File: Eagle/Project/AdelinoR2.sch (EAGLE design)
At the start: 70 parts, among them J1 DC-044-A, J2 YELLOW-8P-2.54, J3 YELLOW-6P-2.54, J4 YELLOW-8P-2.54, J5 YELLOW-8P-2.54, J6 4P-2.0, J7 YELLOW-2X3P-2.54, J8 4P-2.0, Q1 NCE3407A, Q2 CJ2305, SW1 TS-1101F, U1 MP1496DJ-SOT23-8, U2 CJT1117-3.3-SOT223, U3 ESP-12F / OPL: 317060163 / SM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, U4 ATMEGA32U4-MUR-QFN44, U5 74VHC125MTCX-TSSOP14, U6 ATMEGA32U4-TQFP44, X1 306010049_XTAL_16MHZ-3225_4P

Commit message: Power supply routing wip.
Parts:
- removed L3: 303010525_22UH_7.1X6.6MM, Seeed-OPL-2017-01-Inductor-Akita:303010525_22UH_7.1X6.6MM
- removed R14: 10K / 1%, Seeed-Resistor:SMD-RES-10K-1%-1/10W(0603)
- removed R16: 30K / 1%, Seeed-Resistor:SMD-RES-30K-1%-1/10W(0603)
- L2: device Seeed-Inductor:SMD-INDUCTOR-10UH-225MA-10%(0806) -> Seeed-Inductor:SMD-INDUCTOR-10UH-20%-2.35A(2P-5X5X4MM)
- R13: value 68K / 1% -> 2K7 / 1%; device Seeed-Resistor:SMD-RES-68K-1%-1/10W(0603) -> Seeed-Resistor:SMD-RES-2.7K-1%-1/10W(0603); R (none) -> 2K7 / 1%
- R15: device Seeed-Resistor:SMD-RES-3K-1%-1/10W(0603) -> Seeed-Resistor:SMD-RES-510R-1%-1/10W(0603); R (none) -> 510R / 1%
- R18: value 3K / 1% -> 3.3K; device Seeed-Resistor:SMD-RES-3K-1%-1/10W(0603) -> Seeed-Resistor:SMD-RES-3.3K-5%-1/16W(0402)
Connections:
- net N$10 renamed SW_VCC_IN
- net N$12 renamed SW_VCAP
- net N$14 renamed SW_BS
- net N$19 renamed SW_VCC_OUT
- net N$20 renamed SW_EN
- net N$24 renamed SW_FB
- net N$4 renamed SW_SS
- removed net N$21: R16.1, R18.2
- removed net N$22: R14.1, R15.2
- net N$23: now also R15.2, R18.2; no longer R14.2, R16.2
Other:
- moved on the sheet: R15
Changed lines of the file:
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@@
 <setting verticaltext="up"/>
 </settings>
-<grid distance="0.05" unitdist="inch" unit="inch" style="lines" multiple="1" display="no" altdistance="0.01" altunitdist="inch" altunit="inch"/>
+<grid distance="0.1" unitdist="inch" unit="inch" style="lines" multiple="1" display="no" altdistance="0.01" altunitdist="inch" altunit="inch"/>
 <layers>
 <layer number="1" name="Top" color="4" fill="1" visible="no" active="no"/>
@@
 <classes>
 <class number="0" name="default" width="0.254" drill="0.6096">
-<clearance class="0" value="0.254"/>
+<clearance class="0" value="0.2032"/>
 </class>
 </classes>
@@
 <part name="R6" library="Seeed-Resistor" deviceset="SMD-RES-10R-1%-1/16W(0402)" device="" value="10R 1/16W"/>
 <part name="C5" library="Seeed-Capacitor" deviceset="CERAMIC-100NF-25V-10%-X7R(0402)" device="" value="100nf"/>
-<part name="L2" library="Seeed-Inductor" deviceset="SMD-INDUCTOR-10UH-225MA-10%(0806)" device="" value="10UH-225MA"/>
+<part name="L2" library="Seeed-Inductor" deviceset="SMD-INDUCTOR-10UH-20%-2.35A(2P-5X5X4MM)" device="" value="10UH-225MA"/>
 <part name="R7" library="Seeed-Resistor" deviceset="SMD-RES-100K-1%-1/16W(0402)" device="" value="100K"/>
-<part name="R13" library="Seeed-Resistor" deviceset="SMD-RES-68K-1%-1/10W(0603)" device="" value="68K / 1%"/>
-<part name="R14" library="Seeed-Resistor" deviceset="SMD-RES-10K-1%-1/10W(0603)" device="" value="10K / 1%"/>
+<part name="R13" library="Seeed-Resistor" deviceset="SMD-RES-2.7K-1%-1/10W(0603)" device="" value="2K7 / 1%">
+<attribute name="R" value="2K7 / 1%"/>
+</part>
 <part name="GND15" library="supply1" library_urn="urn:adsk.eagle:library:371" deviceset="GND" device=""/>
-<part name="R16" library="Seeed-Resistor" deviceset="SMD-RES-30K-1%-1/10W(0603)" device="" value="30K / 1%"/>
 <part name="C19" library="Seeed-Capacitor" deviceset="CERAMIC-10UF-25V-10%-X5R(0805)" device="" value="10uf"/>
 <part name="C20" library="Seeed-Capacitor" deviceset="CERAMIC-10UF-25V-10%-X5R(0805)" device="" value="10uf"/>
-<part name="R15" library="Seeed-Resistor" deviceset="SMD-RES-3K-1%-1/10W(0603)" device="" value="3K / 1%"/>
-<part name="R18" library="Seeed-Resistor" deviceset="SMD-RES-3K-1%-1/10W(0603)" device="" value="3K / 1%"/>
+<part name="R15" library="Seeed-Resistor" deviceset="SMD-RES-510R-1%-1/10W(0603)" device="" value="3K / 1%">
+<attribute name="R" value="510R / 1%"/>
+</part>
+<part name="R18" library="Seeed-Resistor" deviceset="SMD-RES-3.3K-5%-1/16W(0402)" device="" value="3.3K"/>
 <part name="U6" library="Seeed-IC" deviceset="MCU-ATMEGA32U4-AU(TQFP44)" device="" value="ATMEGA32U4-TQFP44">
 <attribute name="DESC" value="SOCKET B - TQFP44"/>
 </part>
-<part name="L3" library="Seeed-OPL-2017-01-Inductor-Akita" deviceset="303010525_22UH_7.1X6.6MM" device=""/>
 <part name="GND2" library="supply1" library_urn="urn:adsk.eagle:library:371" deviceset="GND" device=""/>
 <part name="P+8" library="supply1" library_urn="urn:adsk.eagle:library:371" deviceset="+5V" device=""/>
@@
 <attribute name="VALUE" x="-123.19" y="148.59" size="1.27" layer="96" ratio="10" rot="R90"/>
 </instance>
-<instance part="L2" gate="L" x="-113.03" y="143.51" smashed="yes">
+<instance part="L2" gate="G$1" x="-113.03" y="143.51" smashed="yes">
 <attribute name="NAME" x="-116.84" y="144.78" size="1.27" layer="95" ratio="10"/>
-<attribute name="VALUE" x="-116.84" y="140.97" size="1.27" layer="96" ratio="10"/>
 </instance>
 <instance part="R7" gate="G$1" x="-170.18" y="143.51" smashed="yes" rot="R180">
@@
 <instance part="R13" gate="G$1" x="-113.03" y="137.16" smashed="yes">
 <attribute name="NAME" x="-116.84" y="138.43" size="1.27" layer="95" ratio="10"/>
-<attribute name="VALUE" x="-116.84" y="134.62" size="1.27" layer="96" ratio="10"/>
-</instance>
-<instance part="R14" gate="G$1" x="-134.62" y="128.27" smashed="yes">
-<attribute name="NAME" x="-138.43" y="129.54" size="1.27" layer="95" ratio="10"/>
-<attribute name="VALUE" x="-138.43" y="125.73" size="1.27" layer="96" ratio="10"/>
+<attribute name="R" x="-116.84" y="134.62" size="1.27" layer="96"/>
 </instance>
 <instance part="GND15" gate="1" x="-152.4" y="115.57" smashed="yes">
 <attribute name="VALUE" x="-154.94" y="113.03" size="1.778" layer="96"/>
-</instance>
-<instance part="R16" gate="G$1" x="-125.73" y="137.16" smashed="yes">
-<attribute name="NAME" x="-129.54" y="138.43" size="1.27" layer="95" ratio="10"/>
-<attribute name="VALUE" x="-129.54" y="134.62" size="1.27" layer="96" ratio="10"/>
 </instance>
 <instance part="C19" gate="G$1" x="-99.06" y="137.16" smashed="yes" rot="R90">
@@
 <attribute name="VALUE" x="-91.44" y="134.62" size="1.27" layer="96" ratio="10"/>
 </instance>
-<instance part="R15" gate="G$1" x="-144.78" y="128.27" smashed="yes">
-<attribute name="NAME" x="-148.59" y="129.54" size="1.27" layer="95" ratio="10"/>
-<attribute name="VALUE" x="-148.59" y="125.73" size="1.27" layer="96" ratio="10"/>
+<instance part="R15" gate="G$1" x="-134.62" y="128.27" smashed="yes">
+<attribute name="NAME" x="-138.43" y="129.54" size="1.27" layer="95" ratio="10"/>
+<attribute name="R" x="-138.43" y="125.73" size="1.27" layer="96"/>
 </instance>
 <instance part="R18" gate="G$1" x="-134.62" y="137.16" smashed="yes">
@@
 <attribute name="VALUE" x="201.93" y="135.89" size="1.778" layer="96"/>
 <attribute name="DESC" x="201.93" y="133.35" size="1.778" layer="96"/>
-</instance>
-<instance part="L3" gate="G$1" x="-137.16" y="165.1" smashed="yes">
-<attribute name="NAME" x="-142.24" y="167.64" size="1.778" layer="97"/>
-<attribute name="VALUE" x="-142.24" y="162.56" size="1.778" layer="96"/>
 </instance>
 <instance part="GND2" gate="1" x="163.83" y="50.8" smashed="yes">
@@
 <junction x="-99.06" y="121.92"/>
 <pinref part="R15" gate="G$1" pin="1"/>
-<wire x1="-148.59" y1="128.27" x2="-152.4" y2="128.27" width="0.1524" layer="91"/>
+<wire x1="-138.43" y1="128.27" x2="-152.4" y2="128.27" width="0.1524" layer="91"/>
 <junction x="-152.4" y="128.27"/>
 <pinref part="C3" gate="G$1" pin="1"/>
@@
 <wire x1="-92.71" y1="143.51" x2="-86.36" y2="143.51" width="0.1524" layer="91"/>
 <junction x="-86.36" y="143.51"/>
-<pinref part="L2" gate="L" pin="2"/>
+<pinref part="L2" gate="G$1" pin="2"/>
 <wire x1="-107.95" y1="143.51" x2="-105.41" y2="143.51" width="0.1524" layer="91"/>
 <wire x1="-105.41" y1="143.51" x2="-99.06" y2="143.51" width="0.1524" layer="91"/>
@@
 </segment>
 </net>
-<net name="N$10" class="0">
+<net name="SW_VCC_IN" class="0">
 <segment>
 <pinref part="Q1" gate="G$1" pin="S"/>
@@
 </segment>
 </net>
-<net name="N$12" class="0">
+<net name="SW_VCAP" class="0">
 <segment>
 <pinref part="U1" gate="G$1" pin="VCC"/>
@@
 </segment>
 </net>
-<net name="N$14" class="0">
+<net name="SW_BS" class="0">
 <segment>
 <pinref part="U1" gate="G$1" pin="BS"/>
@@
 </segment>
 </net>
-<net name="N$19" class="0">
+<net name="SW_VCC_OUT" class="0">
 <segment>
 <pinref part="U1" gate="G$1" pin="SW"/>
-<pinref part="L2" gate="L" pin="1"/>
+<pinref part="L2" gate="G$1" pin="1"/>
 <wire x1="-140.97" y1="143.51" x2="-119.38" y2="143.51" width="0.1524" layer="91"/>
 <pinref part="C5" gate="G$1" pin="1"/>
@@
 <wire x1="-119.38" y1="147.32" x2="-119.38" y2="143.51" width="0.1524" layer="91"/>
 <junction x="-119.38" y="143.51"/>
-</segment>
-</net>
-<net name="N$20" class="0">
+<label x="-128.27" y="143.51" size="0.8128" layer="95"/>
+</segment>
+</net>
+<net name="SW_EN" class="0">
 <segment>
 <pinref part="U1" gate="G$1" pin="EN/SYNC"/>
@@
 <net name="N$23" class="0">
 <segment>
-<pinref part="R16" gate="G$1" pin="2"/>
 <pinref part="R13" gate="G$1" pin="1"/>
-<wire x1="-116.84" y1="137.16" x2="-119.38" y2="137.16" width="0.1524" layer="91"/>
-<pinref part="R14" gate="G$1" pin="2"/>
-<wire x1="-119.38" y1="137.16" x2="-121.92" y2="137.16" width="0.1524" layer="91"/>
+<pinref part="R18" gate="G$1" pin="2"/>
+<wire x1="-130.81" y1="137.16" x2="-119.38" y2="137.16" width="0.1524" layer="91"/>
+<pinref part="R15" gate="G$1" pin="2"/>
+<wire x1="-119.38" y1="137.16" x2="-116.84" y2="137.16" width="0.1524" layer="91"/>
 <wire x1="-130.81" y1="128.27" x2="-119.38" y2="128.27" width="0.1524" layer="91"/>
 <wire x1="-119.38" y1="128.27" x2="-119.38" y2="137.16" width="0.1524" layer="91"/>
@@
 </segment>
 </net>
-<net name="N$22" class="0">
-<segment>
-<pinref part="R14" gate="G$1" pin="1"/>
-<pinref part="R15" gate="G$1" pin="2"/>
-<wire x1="-138.43" y1="128.27" x2="-140.97" y2="128.27" width="0.1524" layer="91"/>
-</segment>
-</net>
-<net name="N$4" class="0">
+<net name="SW_SS" class="0">
 <segment>
 <pinref part="C3" gate="G$1" pin="2"/>
@@
 </segment>
 </net>
-<net name="N$21" class="0">
-<segment>
-<pinref part="R16" gate="G$1" pin="1"/>
-<pinref part="R18" gate="G$1" pin="2"/>
-<wire x1="-129.54" y1="137.16" x2="-130.81" y2="137.16" width="0.1524" layer="91"/>
-</segment>
-</net>
-<net name="N$24" class="0">
+<net name="SW_FB" class="0">
 <segment>
 <pinref part="R18" gate="G$1" pin="1"/>

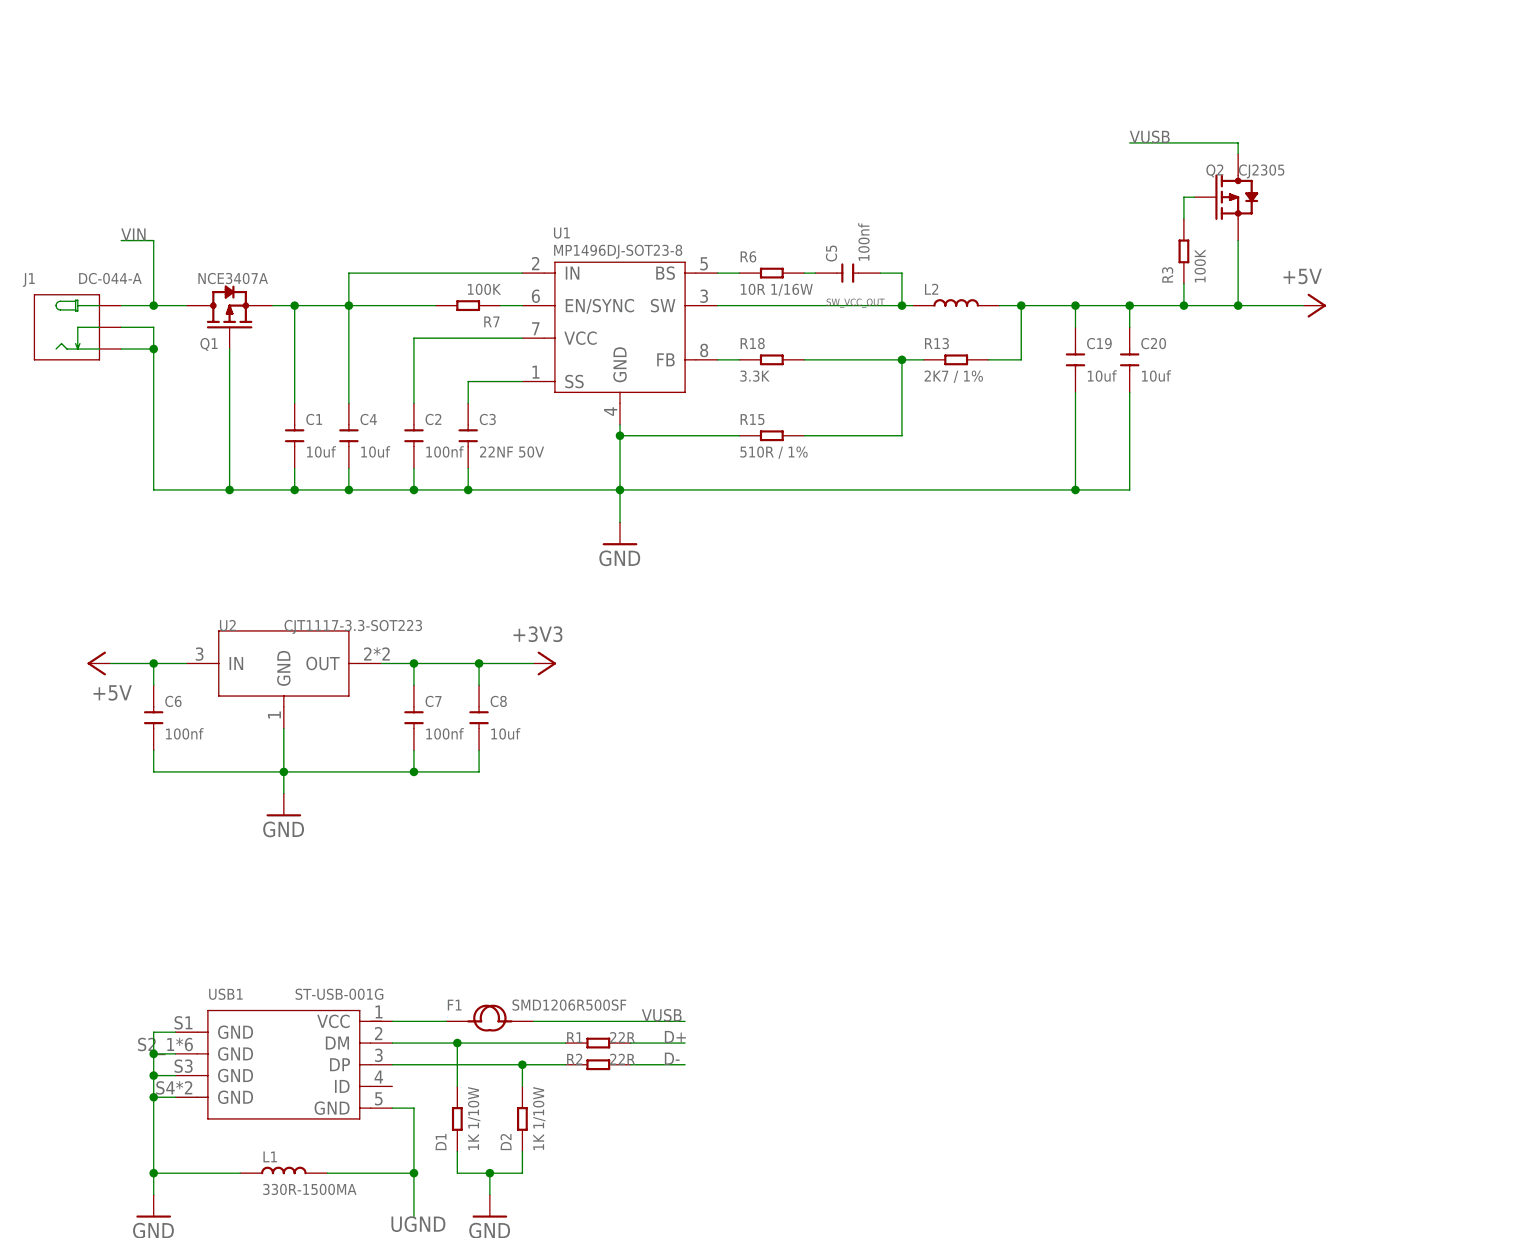
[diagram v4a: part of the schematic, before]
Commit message: Add TVS to protect power input.
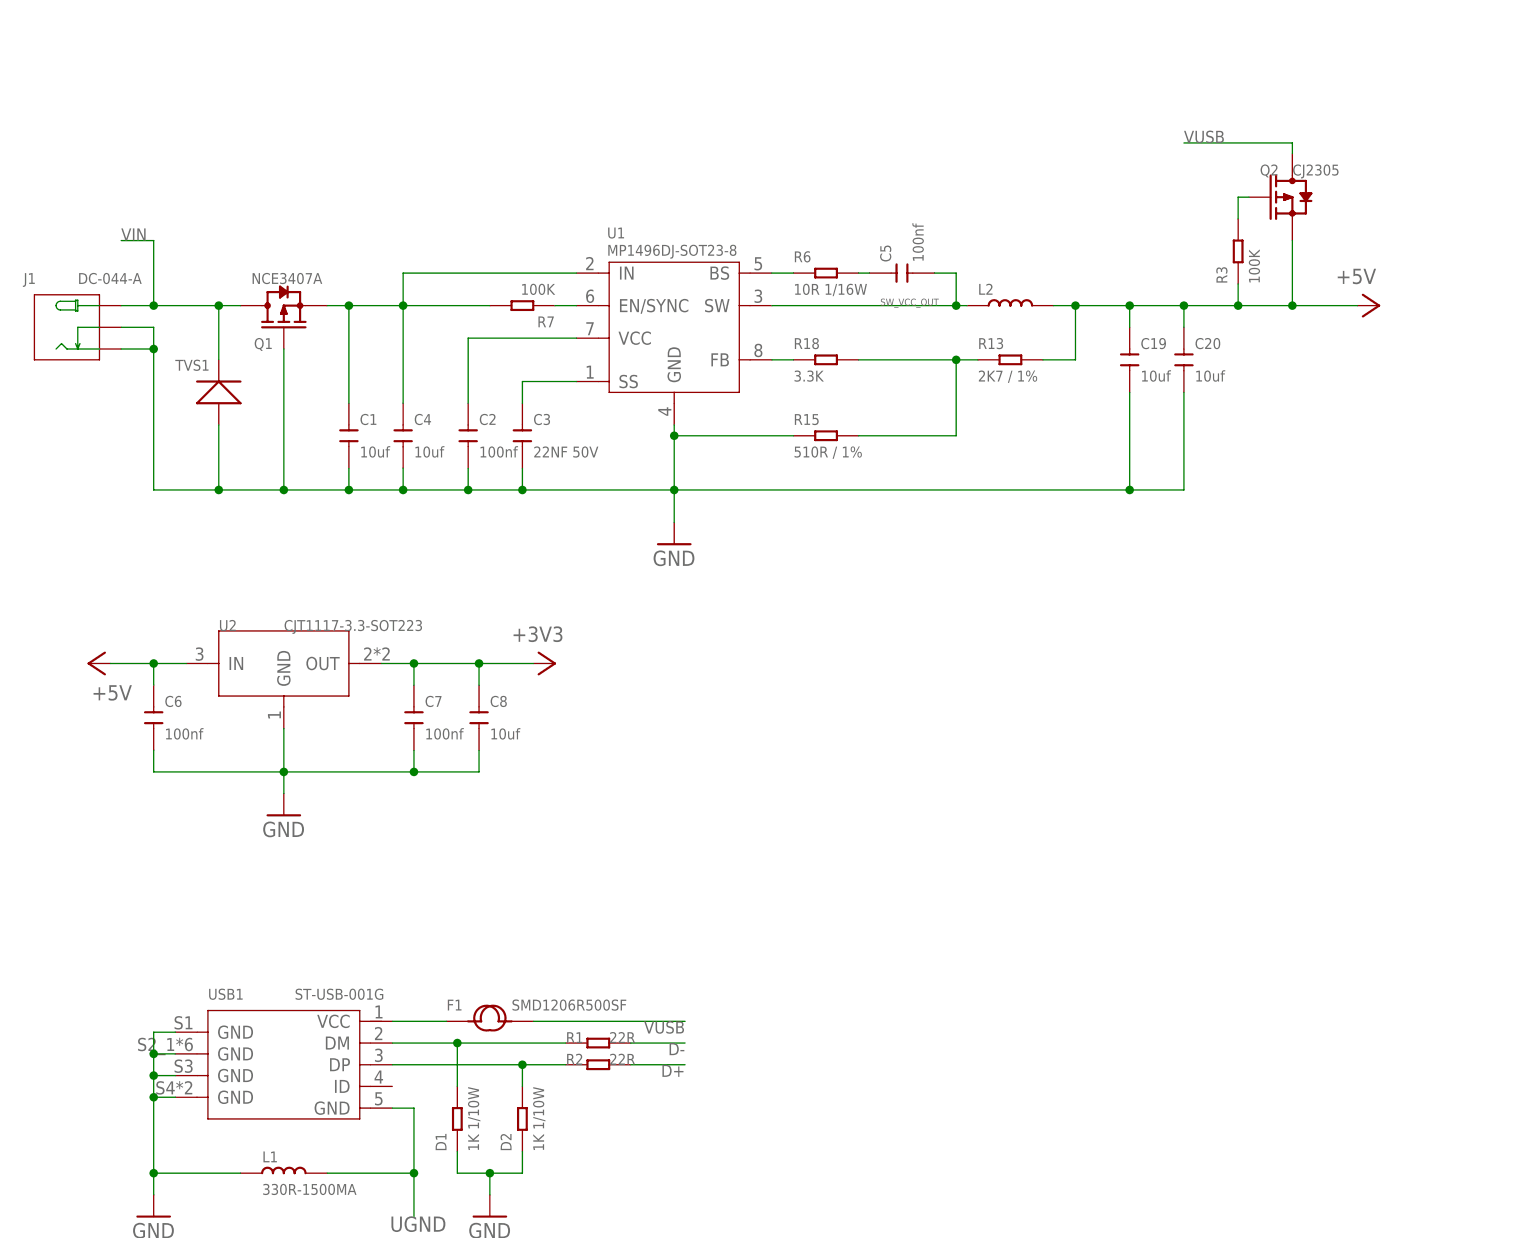
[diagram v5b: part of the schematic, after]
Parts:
- added TVS1: (no value), Seeed-OPL-2017-01-Diode-james:SMD-DIODE-TVS-7VWM-22.7VC-SOD-523
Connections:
- net D+: now also R2.2; no longer R1.2
- net D-: now also R1.2; no longer R2.2
- net GND: now also TVS1.+
- net VIN: now also TVS1.-
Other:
- moved on the sheet: C1, C19, C2, C20, C3, C4, C5, L2, Q1, Q2, R13, R15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

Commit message: Wip.
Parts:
- added D10, D9: YEL-0603, Seeed-LED:SMD-LED-CLEAR-YELLOW(0603)
- added D11: 20V-500MA, Seeed-Diode:SMD-DIODE-SCHOTTKY-20V-500MA(SOD-123)P
- added D3: GRE-0603, Seeed-LED:SMD-LED-CLEAR-GREEN(0603)
- added R14, R16, R21, R22: 1K, Seeed-Resistor:SMD-RES-1K-5%-1/16W(0402)
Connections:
- net MISO renamed AT_MISO
- net MOSI renamed AT_MOSI
- net SCK renamed AT_SCK
- new net AT_SS: U4.PB0(SS/PCINT0), U6.PB0(SS/PCINT0)
- new net N$10: D10.+, R16.2
- new net N$4: D3.+, R21.2
- new net N$7: D11.+, D9.+, R22.2
- net +5V: now also R21.1
- net ACT_LED: now also R22.1, U4.PD5(XCLK1/!CTS), U6.PD5(XCLK1/!CTS); no longer U4.PB0(SS/PCINT0), U6.PB0(SS/PCINT0)
- net BOOT_MODE: now also R14.2
- net ESP_EN: now also U4.PE2(!HWB), U6.PE2(!HWB); no longer U4.PD5(XCLK1/!CTS), U6.PD5(XCLK1/!CTS)
- net GND: now also D10.-, D3.-, D9.-
- net PIN_D13: now also R14.1, R16.1
- net RSTAT: now also D11.-; no longer U4.PE2(!HWB), U6.PE2(!HWB)

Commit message: Wip.
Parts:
- removed D4, D5: YEL-0603, Seeed-LED:SMD-LED-CLEAR-YELLOW(0603)
- removed D6: GRE-0603, Seeed-LED:SMD-LED-CLEAR-GREEN(0603)
- removed U5: 74VHC125MTCX-TSSOP14, Seeed-IC:LOGIC-74VHC125MTCX(TSSOP14)
- added R23, R24, R25, R26: 1K, Seeed-Resistor:SMD-RES-1K-5%-1/16W(0402)
- added R27: 470R, Seeed-Resistor:SMD-RES-470R-5%-1/16W(0402)
- added R28: 10K, Seeed-Resistor:SMD-RES-10K-1%-1/16W(0402)
- added R29: 0R, Seeed-Resistor:SMD-RES-0R-5%-1/16W(0402)
- R10, R5: value 10K 1/16W -> 10K
- R11, R12: value 1K -> 10K; device Seeed-Resistor:SMD-RES-ARRAY-1K-4R(RA1206-8) -> Seeed-Resistor:SMD-RES-10K-1%-1/16W(0402)
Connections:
- removed net CH_EN: U3.EN, U5.O2
- removed net D13_LED: R11.6, U5.O3
- removed net GPIO15_PD: R12.4, U3.GPIO15
- removed net GPIO2: R11.5
- removed net GPIO2_PU: R12.2, U3.GPIO2
- removed net HSPI_CLK: U3.GPIO14
- removed net HSPI_MISO: U3.GPIO12
- removed net HSPI_MOSI: U3.GPIO13
- removed net N$11: D6.-, R11.1
- removed net N$16: R12.3
- removed net N$8: D5.-, R11.2
- removed net RESET_AT: U3.GPIO16, U5.!A0, U5.B0
- removed net RST_PU: R12.1, U3.RST
- new net GPIO2_LED: D8.-, R28.2, U3.GPIO2
- new net N$12: R23.2, U3.GPIO12
- new net N$14: R24.2, U3.GPIO13
- new net N$19: R25.2, U3.GPIO14
- new net N$20: R12.2, R26.2, U3.GPIO15
- new net N$22: R10.2, U3.RST
- net +3V3: now also R10.1, R11.2, R27.1, R28.1, R5.1; no longer D8.+, R12.6, R12.7, R12.8
- net +5V: no longer D4.+, D5.+, D6.+, R10.2, R5.2, U5.VCC
- net ACT_LED: no longer R11.7
- net AT_MISO: now also R23.1
- net AT_MOSI: now also R24.1; no longer R10.1, U5.B1
- net AT_SCK: now also R25.1
- net AT_SS: now also R26.1
- net BOOT_MODE: now also R11.1; no longer U5.O1
- net ESP_EN: now also R5.2, U3.EN; no longer R5.1, U5.B2
- net GND: now also R12.1; no longer R11.8, R12.5, U5.!A1, U5.!A2, U5.!A3, U5.GND
- net N$5: now also R29.2, U3.GPIO16; no longer D8.-, R11.4
- net N$6: now also D8.+, R27.2; no longer D4.-, R11.3
- net PIN_D0: now also J8.1
- net PIN_D1: now also J8.2
- net PIN_D10: no longer J8.1
- net PIN_D13: no longer U5.B3
- net PIN_D2: now also U3.GPIO4; no longer U3.GPIO5
- net PIN_D3: now also U3.GPIO5; no longer U3.GPIO4
- net PIN_D9: no longer J8.2
- net RESET: now also R29.1; no longer U5.O0
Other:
- note added: "ESP-12F & LEDs"
- note added: "Grove I2C"
- note added: "Grove Serial"
- note added: "I/O PINS"
- note removed: "ESP-12F"
- note removed: "I/O PINS & LEDS"
- moved on the sheet: D10, D11, D3, D8, D9, J6, J7, J8, R10, R14, R16, R21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
